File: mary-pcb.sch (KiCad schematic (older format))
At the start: 69 parts, among them SW1 SW_Push, SW2 Rotary_Encoder_Switch, U1 ATmega32U4-AU, Y1 16MHz

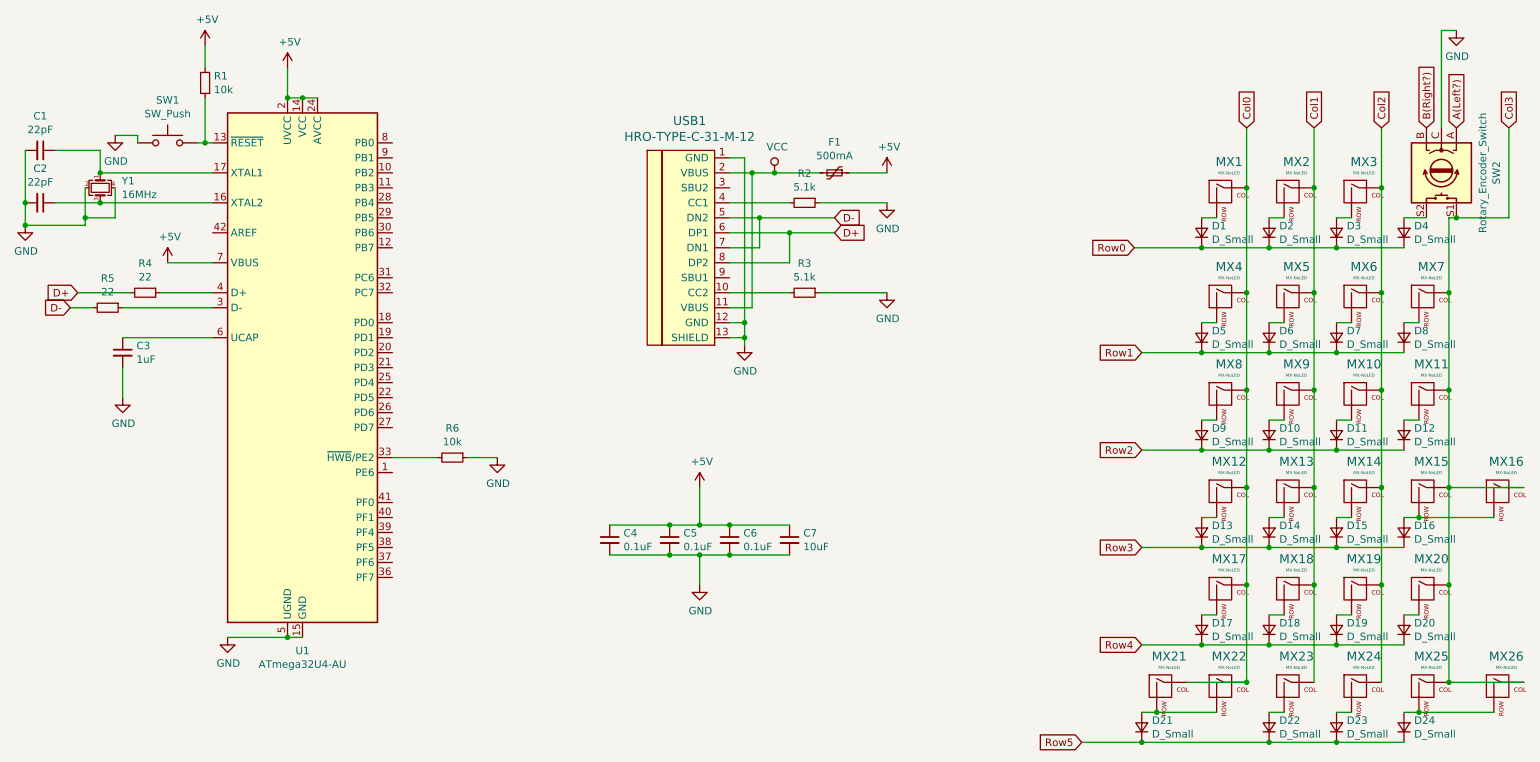
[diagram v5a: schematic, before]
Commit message: complete routing
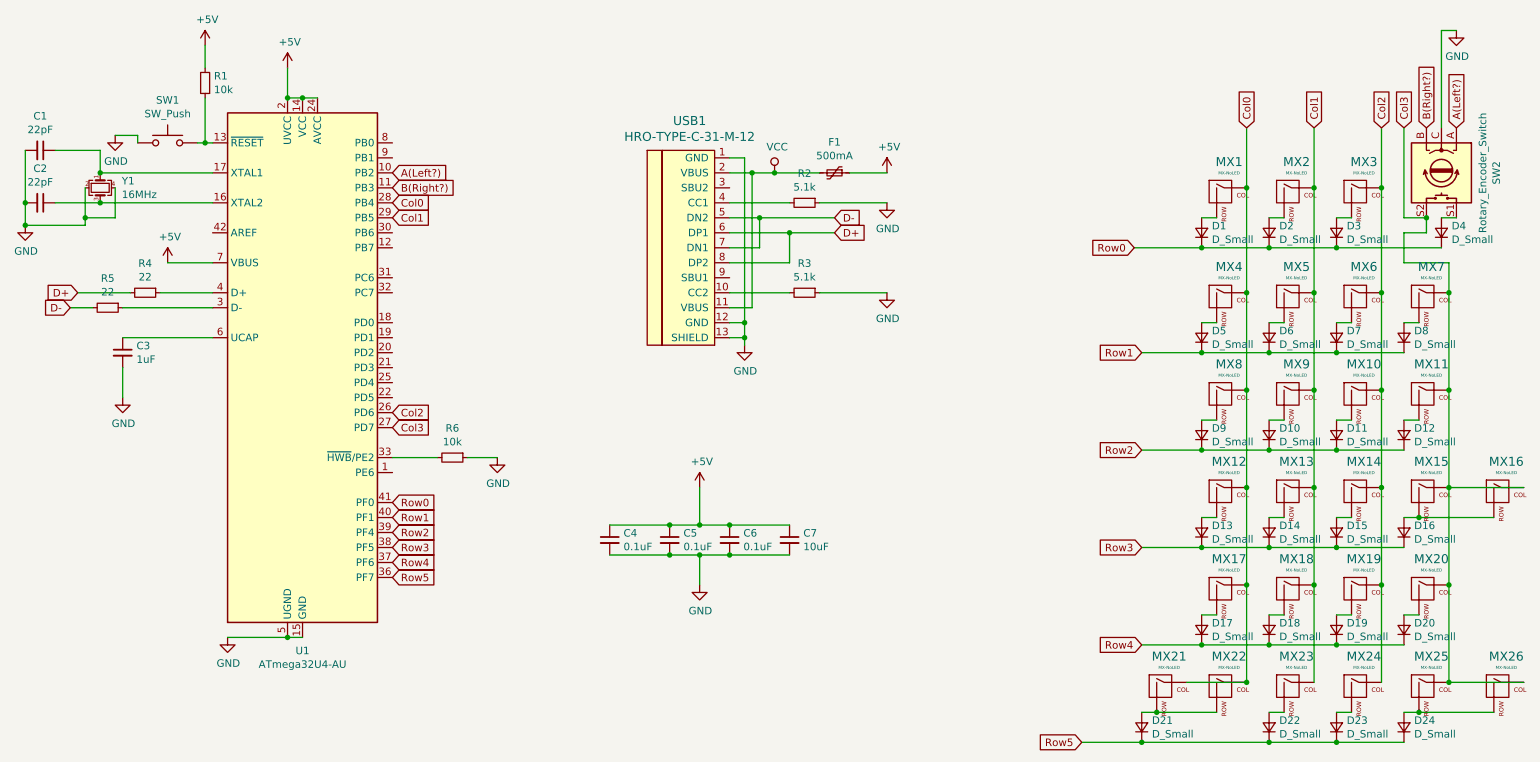
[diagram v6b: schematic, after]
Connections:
- net A(Left?): now also U1.10 (PB2)
- net B(Right?): now also U1.11 (PB3)
- net Col0: now also U1.28 (PB4)
- net Col1: now also U1.29 (PB5)
- net Col2: now also U1.26 (PD6)
- net Col3: now also SW2.S2, U1.27 (PD7); no longer SW2.S1
- net Row0: now also U1.41 (PF0)
- net Row1: now also U1.40 (PF1)
- net Row2: now also U1.39 (PF4)
- net Row3: now also U1.38 (PF5)
- net Row4: now also U1.37 (PF6)
- net Row5: now also U1.36 (PF7)
- net at D4.2 (A): now also SW2.S1; no longer SW2.S2
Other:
- moved on the sheet: D4
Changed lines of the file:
@@
 	0    1    1    0
 $EndComp
-$Comp
-L Device:D_Small D4
-U 1 1 5E3ADAEC
-P 10200 2050
-F 0 "D4" V 10246 1982 50  0000 R CNN
-F 1 "D_Small" V 10155 1982 50  0000 R CNN
-F 2 "Diode_SMD:D_SOD-123" V 10200 2050 50  0001 C CNN
-F 3 "~" V 10200 2050 50  0001 C CNN
-	1    10200 2050
-	0    -1   -1   0
-$EndComp
-Wire Wire Line
-	10350 1950 10200 1950
-Wire Wire Line
-	9750 2150 10200 2150
 Connection ~ 9750 2150
-Wire Wire Line
-	10550 1950 10900 1950
-Wire Wire Line
-	10900 1950 10900 1350
-Wire Wire Line
-	10550 1950 10500 1950
-Wire Wire Line
-	10500 1950 10500 2450
-Connection ~ 10550 1950
-Connection ~ 10500 2450
 Wire Wire Line
 	10500 2450 10500 3100
@@
 Text GLabel 10050 1350 1    50   Input ~ 0
 Col2
-Text GLabel 10900 1350 1    50   Input ~ 0
+Text GLabel 10200 1350 1    50   Input ~ 0
 Col3
 Text GLabel 10350 1350 1    50   Input ~ 0
@@
 Wire Wire Line
 	10450 700  10450 1350
+Wire Wire Line
+	9750 2150 10450 2150
+Wire Wire Line
+	10200 2250 10500 2250
+Wire Wire Line
+	10500 2250 10500 2450
+Connection ~ 10500 2450
+Text GLabel 3450 3850 2    50   Input ~ 0
+Row0
+Text GLabel 3450 3950 2    50   Input ~ 0
+Row1
+Text GLabel 3450 4050 2    50   Input ~ 0
+Row2
+Text GLabel 3450 4150 2    50   Input ~ 0
+Row3
+Text GLabel 3450 4250 2    50   Input ~ 0
+Row4
+Text GLabel 3450 4350 2    50   Input ~ 0
+Row5
+Text GLabel 3450 1850 2    50   Input ~ 0
+Col0
+Text GLabel 3450 1950 2    50   Input ~ 0
+Col1
+Text GLabel 3450 3250 2    50   Input ~ 0
+Col2
+Text GLabel 3450 3350 2    50   Input ~ 0
+Col3
+$Comp
+L Device:D_Small D4
+U 1 1 5E3ADAEC
+P 10450 2050
+F 0 "D4" V 10496 1982 50  0000 R CNN
+F 1 "D_Small" V 10405 1982 50  0000 R CNN
+F 2 "Diode_SMD:D_SOD-123" V 10450 2050 50  0001 C CNN
+F 3 "~" V 10450 2050 50  0001 C CNN
+	1    10450 2050
+	0    -1   -1   0
+$EndComp
+Wire Wire Line
+	10450 1950 10550 1950
+Wire Wire Line
+	10200 1350 10200 1950
+Wire Wire Line
+	10200 1950 10350 1950
+Wire Wire Line
+	10200 2250 10200 2050
+Wire Wire Line
+	10200 2050 10350 2050
+Wire Wire Line
+	10350 2050 10350 1950
+Connection ~ 10350 1950
+Text GLabel 3450 1650 2    50   Input ~ 0
+A(Left?)
+Text GLabel 3450 1750 2    50   Input ~ 0
+B(Right?)
 $EndSCHEMATC

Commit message: complete routing, upload renders
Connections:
- net A(Left?): now also U1.21 (PD3); no longer U1.10 (PB2)
- net B(Right?): now also U1.22 (PD5); no longer U1.11 (PB3)
- net Row0: now also U1.36 (PF7); no longer U1.41 (PF0)
- net Row1: now also U1.37 (PF6); no longer U1.40 (PF1)
- net Row2: now also U1.38 (PF5); no longer U1.39 (PF4)
- net Row3: now also U1.39 (PF4); no longer U1.38 (PF5)
- net Row4: now also U1.40 (PF1); no longer U1.37 (PF6)
- net Row5: now also U1.41 (PF0); no longer U1.36 (PF7)
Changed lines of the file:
@@
 	10500 2250 10500 2450
 Connection ~ 10500 2450
-Text GLabel 3450 3850 2    50   Input ~ 0
-Row0
-Text GLabel 3450 3950 2    50   Input ~ 0
-Row1
-Text GLabel 3450 4050 2    50   Input ~ 0
-Row2
-Text GLabel 3450 4150 2    50   Input ~ 0
-Row3
-Text GLabel 3450 4250 2    50   Input ~ 0
-Row4
-Text GLabel 3450 4350 2    50   Input ~ 0
-Row5
-Text GLabel 3450 1850 2    50   Input ~ 0
-Col0
-Text GLabel 3450 1950 2    50   Input ~ 0
-Col1
-Text GLabel 3450 3250 2    50   Input ~ 0
-Col2
-Text GLabel 3450 3350 2    50   Input ~ 0
-Col3
 $Comp
 L Device:D_Small D4
@@
 	10350 2050 10350 1950
 Connection ~ 10350 1950
-Text GLabel 3450 1650 2    50   Input ~ 0
+Text GLabel 3450 3850 2    50   Input ~ 0
+Row5
+Text GLabel 3450 3950 2    50   Input ~ 0
+Row4
+Text GLabel 3450 4050 2    50   Input ~ 0
+Row3
+Text GLabel 3450 4150 2    50   Input ~ 0
+Row2
+Text GLabel 3450 4250 2    50   Input ~ 0
+Row1
+Text GLabel 3450 4350 2    50   Input ~ 0
+Row0
+Text GLabel 3450 1850 2    50   Input ~ 0
+Col0
+Text GLabel 3450 3350 2    50   Input ~ 0
+Col3
+Text GLabel 3450 3250 2    50   Input ~ 0
+Col2
+Text GLabel 3450 1950 2    50   Input ~ 0
+Col1
+Text GLabel 3450 2950 2    50   Input ~ 0
 A(Left?)
-Text GLabel 3450 1750 2    50   Input ~ 0
+Text GLabel 3450 3150 2    50   Input ~ 0
 B(Right?)
 $EndSCHEMATC

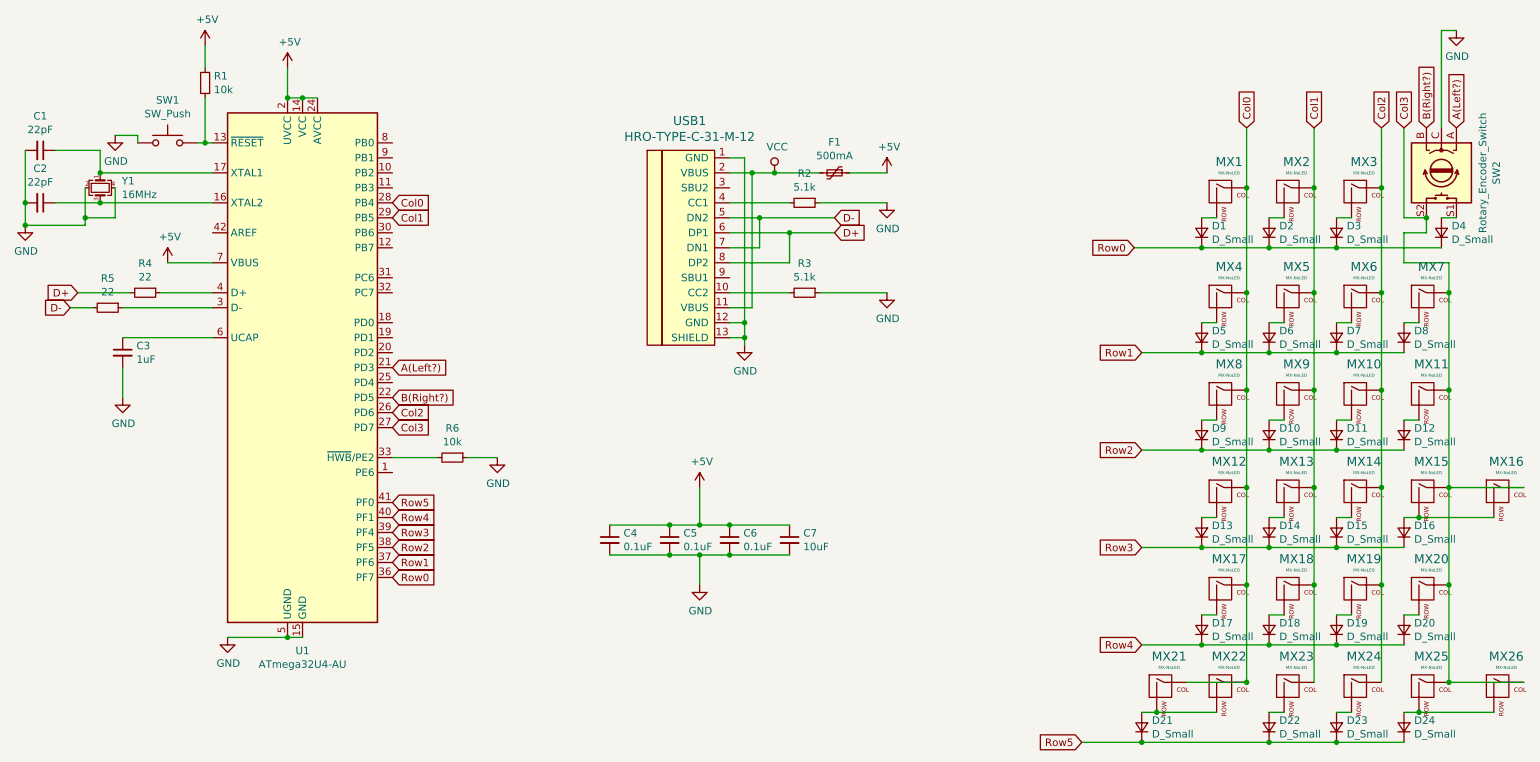
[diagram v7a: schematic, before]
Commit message: add esd protection, ground pours, via stitching
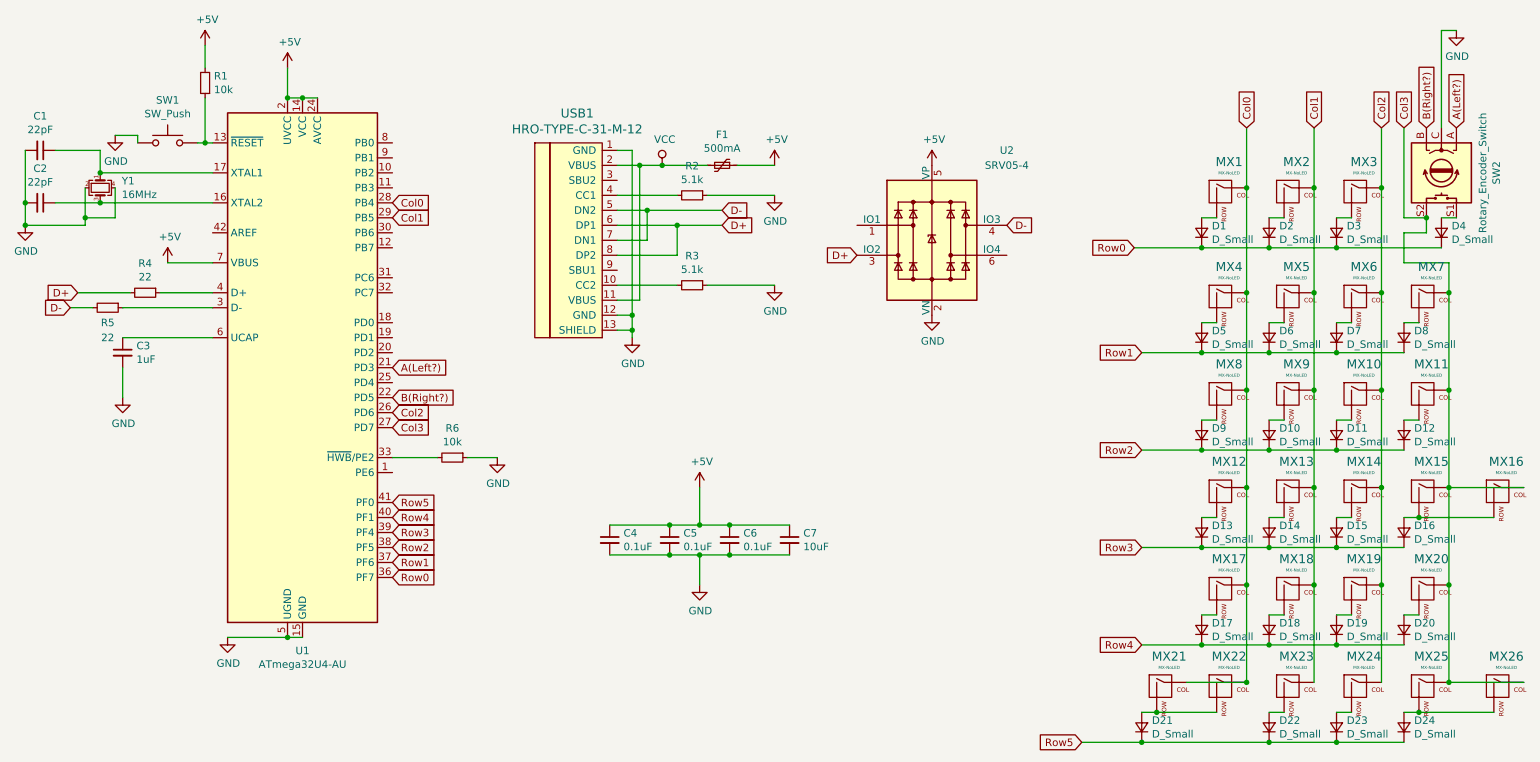
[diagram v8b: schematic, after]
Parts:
- added U2: SRV05-4, Package_TO_SOT_SMD:SOT-23-6, symbol Power_Protection:SRV05-4
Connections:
- net +5V: now also U2.5 (VP)
- net D+: now also U2.3 (IO2)
- net D-: now also U2.4 (IO3)
- net GND: now also U2.2 (VN)
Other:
- moved on the sheet: F1, R2, R3, USB1
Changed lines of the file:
@@
 U 1 1 5E0D915D
 P 1550 2550
-F 0 "R5" V 1354 2550 50  0000 C CNN
-F 1 "22" V 1445 2550 50  0000 C CNN
+F 0 "R5" V 1650 2550 50  0000 C CNN
+F 1 "22" V 1750 2550 50  0000 C CNN
 F 2 "Resistor_SMD:R_0805_2012Metric" H 1550 2550 50  0001 C CNN
 F 3 "~" H 1550 2550 50  0001 C CNN
@@
 L Type-C:HRO-TYPE-C-31-M-12 USB1
 U 1 1 5E154775
-P 5600 2100
-F 0 "USB1" H 5433 2897 60  0000 C CNN
-F 1 "HRO-TYPE-C-31-M-12" H 5433 2791 60  0000 C CNN
-F 2 "Type-C:HRO-TYPE-C-31-M-12" H 5600 2100 60  0001 C CNN
-F 3 "" H 5600 2100 60  0001 C CNN
-	1    5600 2100
+P 4850 2050
+F 0 "USB1" H 4683 2847 60  0000 C CNN
+F 1 "HRO-TYPE-C-31-M-12" H 4683 2741 60  0000 C CNN
+F 2 "Type-C:HRO-TYPE-C-31-M-12" H 4850 2050 60  0001 C CNN
+F 3 "" H 4850 2050 60  0001 C CNN
+	1    4850 2050
 	1    0    0    -1
 $EndComp
@@
 L Device:Polyfuse_Small F1
 U 1 1 5E1567C4
-P 6400 1650
-F 0 "F1" V 6195 1650 50  0000 C CNN
-F 1 "500mA" V 6286 1650 50  0000 C CNN
-F 2 "Fuse:Fuse_1206_3216Metric" H 6450 1450 50  0001 L CNN
-F 3 "~" H 6400 1650 50  0001 C CNN
-	1    6400 1650
+P 5650 1600
+F 0 "F1" V 5445 1600 50  0000 C CNN
+F 1 "500mA" V 5536 1600 50  0000 C CNN
+F 2 "Fuse:Fuse_1206_3216Metric" H 5700 1400 50  0001 L CNN
+F 3 "~" H 5650 1600 50  0001 C CNN
+	1    5650 1600
 	0    1    1    0
 $EndComp
@@
 L power:+5V #PWR0109
 U 1 1 5E15A63C
-P 6750 1650
-F 0 "#PWR0109" H 6750 1500 50  0001 C CNN
-F 1 "+5V" H 6765 1823 50  0000 C CNN
-F 2 "" H 6750 1650 50  0001 C CNN
-F 3 "" H 6750 1650 50  0001 C CNN
-	1    6750 1650
-	1    0    0    -1
-$EndComp
-Wire Wire Line
-	5700 1650 5850 1650
-Wire Wire Line
-	6500 1650 6750 1650
+P 6000 1600
+F 0 "#PWR0109" H 6000 1450 50  0001 C CNN
+F 1 "+5V" H 6015 1773 50  0000 C CNN
+F 2 "" H 6000 1600 50  0001 C CNN
+F 3 "" H 6000 1600 50  0001 C CNN
+	1    6000 1600
+	1    0    0    -1
+$EndComp
+Wire Wire Line
+	4950 1600 5100 1600
+Wire Wire Line
+	5750 1600 6000 1600
 $Comp
 L power:VCC #PWR0110
 U 1 1 5E15C909
-P 6000 1650
-F 0 "#PWR0110" H 6000 1500 50  0001 C CNN
-F 1 "VCC" H 6017 1823 50  0000 C CNN
-F 2 "" H 6000 1650 50  0001 C CNN
-F 3 "" H 6000 1650 50  0001 C CNN
-	1    6000 1650
-	1    0    0    -1
-$EndComp
-Connection ~ 6000 1650
-Wire Wire Line
-	6000 1650 6300 1650
-Text GLabel 6400 2050 2    50   Input ~ 0
+P 5250 1600
+F 0 "#PWR0110" H 5250 1450 50  0001 C CNN
+F 1 "VCC" H 5267 1773 50  0000 C CNN
+F 2 "" H 5250 1600 50  0001 C CNN
+F 3 "" H 5250 1600 50  0001 C CNN
+	1    5250 1600
+	1    0    0    -1
+$EndComp
+Connection ~ 5250 1600
+Wire Wire Line
+	5250 1600 5550 1600
+Text GLabel 5650 2000 2    50   Input ~ 0
 D+
 Wire Wire Line
-	5700 2050 6100 2050
-Wire Wire Line
-	5700 2250 6100 2250
-Wire Wire Line
-	6100 2250 6100 2050
-Connection ~ 6100 2050
-Wire Wire Line
-	6100 2050 6400 2050
-Text GLabel 6400 1950 2    50   Input ~ 0
+	4950 2000 5350 2000
+Wire Wire Line
+	4950 2200 5350 2200
+Wire Wire Line
+	5350 2200 5350 2000
+Connection ~ 5350 2000
+Wire Wire Line
+	5350 2000 5650 2000
+Text GLabel 5650 1900 2    50   Input ~ 0
 D-
 Wire Wire Line
-	5700 1950 5900 1950
-Wire Wire Line
-	5700 2150 5900 2150
-Wire Wire Line
-	5900 2150 5900 1950
-Connection ~ 5900 1950
-Wire Wire Line
-	5900 1950 6400 1950
+	4950 1900 5150 1900
+Wire Wire Line
+	4950 2100 5150 2100
+Wire Wire Line
+	5150 2100 5150 1900
+Connection ~ 5150 1900
+Wire Wire Line
+	5150 1900 5650 1900
 $Comp
 L power:GND #PWR0111
 U 1 1 5E164B62
-P 5800 2800
-F 0 "#PWR0111" H 5800 2550 50  0001 C CNN
-F 1 "GND" H 5805 2627 50  0000 C CNN
-F 2 "" H 5800 2800 50  0001 C CNN
-F 3 "" H 5800 2800 50  0001 C CNN
-	1    5800 2800
-	1    0    0    -1
-$EndComp
-Wire Wire Line
-	5700 1550 5800 1550
-Wire Wire Line
-	5800 1550 5800 2650
-Wire Wire Line
-	5700 2650 5800 2650
-Connection ~ 5800 2650
-Wire Wire Line
-	5800 2650 5800 2750
-Wire Wire Line
-	5700 2750 5800 2750
-Connection ~ 5800 2750
-Wire Wire Line
-	5800 2750 5800 2800
-Wire Wire Line
-	5700 2550 5850 2550
-Wire Wire Line
-	5850 2550 5850 1650
-Connection ~ 5850 1650
-Wire Wire Line
-	5850 1650 6000 1650
+P 5050 2750
+F 0 "#PWR0111" H 5050 2500 50  0001 C CNN
+F 1 "GND" H 5055 2577 50  0000 C CNN
+F 2 "" H 5050 2750 50  0001 C CNN
+F 3 "" H 5050 2750 50  0001 C CNN
+	1    5050 2750
+	1    0    0    -1
+$EndComp
+Wire Wire Line
+	4950 1500 5050 1500
+Wire Wire Line
+	5050 1500 5050 2600
+Wire Wire Line
+	4950 2600 5050 2600
+Connection ~ 5050 2600
+Wire Wire Line
+	5050 2600 5050 2700
+Wire Wire Line
+	4950 2700 5050 2700
+Connection ~ 5050 2700
+Wire Wire Line
+	5050 2700 5050 2750
+Wire Wire Line
+	4950 2500 5100 2500
+Wire Wire Line
+	5100 2500 5100 1600
+Connection ~ 5100 1600
+Wire Wire Line
+	5100 1600 5250 1600
 $Comp
 L power:GND #PWR0112
 U 1 1 5E17016B
-P 6750 1850
-F 0 "#PWR0112" H 6750 1600 50  0001 C CNN
-F 1 "GND" H 6755 1677 50  0000 C CNN
-F 2 "" H 6750 1850 50  0001 C CNN
-F 3 "" H 6750 1850 50  0001 C CNN
-	1    6750 1850
+P 6000 1800
+F 0 "#PWR0112" H 6000 1550 50  0001 C CNN
+F 1 "GND" H 6005 1627 50  0000 C CNN
+F 2 "" H 6000 1800 50  0001 C CNN
+F 3 "" H 6000 1800 50  0001 C CNN
+	1    6000 1800
 	1    0    0    -1
 $EndComp
@@
 L Device:R_Small R2
 U 1 1 5E172396
-P 6200 1850
-F 0 "R2" V 6004 1850 50  0000 C CNN
-F 1 "5.1k" V 6095 1850 50  0000 C CNN
-F 2 "Resistor_SMD:R_0805_2012Metric" H 6200 1850 50  0001 C CNN
-F 3 "~" H 6200 1850 50  0001 C CNN
-	1    6200 1850
+P 5450 1800
+F 0 "R2" V 5254 1800 50  0000 C CNN
+F 1 "5.1k" V 5345 1800 50  0000 C CNN
+F 2 "Resistor_SMD:R_0805_2012Metric" H 5450 1800 50  0001 C CNN
+F 3 "~" H 5450 1800 50  0001 C CNN
+	1    5450 1800
 	0    1    1    0
 $EndComp
 Wire Wire Line
-	5700 1850 6100 1850
-Wire Wire Line
-	6300 1850 6750 1850
+	4950 1800 5350 1800
+Wire Wire Line
+	5550 1800 6000 1800
 $Comp
 L Device:R_Small R3
 U 1 1 5E175B75
-P 6200 2450
-F 0 "R3" V 6004 2450 50  0000 C CNN
-F 1 "5.1k" V 6095 2450 50  0000 C CNN
-F 2 "Resistor_SMD:R_0805_2012Metric" H 6200 2450 50  0001 C CNN
-F 3 "~" H 6200 2450 50  0001 C CNN
-	1    6200 2450
+P 5450 2400
+F 0 "R3" V 5254 2400 50  0000 C CNN
+F 1 "5.1k" V 5345 2400 50  0000 C CNN
+F 2 "Resistor_SMD:R_0805_2012Metric" H 5450 2400 50  0001 C CNN
+F 3 "~" H 5450 2400 50  0001 C CNN
+	1    5450 2400
 	0    1    1    0
 $EndComp
@@
 L power:GND #PWR0113
 U 1 1 5E175EA6
-P 6750 2450
-F 0 "#PWR0113" H 6750 2200 50  0001 C CNN
-F 1 "GND" H 6755 2277 50  0000 C CNN
-F 2 "" H 6750 2450 50  0001 C CNN
-F 3 "" H 6750 2450 50  0001 C CNN
-	1    6750 2450
-	1    0    0    -1
-$EndComp
-Wire Wire Line
-	5700 2450 6100 2450
-Wire Wire Line
-	6300 2450 6750 2450
+P 6000 2400
+F 0 "#PWR0113" H 6000 2150 50  0001 C CNN
+F 1 "GND" H 6005 2227 50  0000 C CNN
+F 2 "" H 6000 2400 50  0001 C CNN
+F 3 "" H 6000 2400 50  0001 C CNN
+	1    6000 2400
+	1    0    0    -1
+$EndComp
+Wire Wire Line
+	4950 2400 5350 2400
+Wire Wire Line
+	5550 2400 6000 2400
 Wire Wire Line
 	5500 4000 5300 4000
@@
 Text GLabel 3450 3150 2    50   Input ~ 0
 B(Right?)
+$Comp
+L Power_Protection:SRV05-4 U2
+U 1 1 5E6936CC
+P 7050 2100
+F 0 "U2" H 7550 2700 50  0000 C CNN
+F 1 "SRV05-4" H 7550 2600 50  0000 C CNN
+F 2 "Package_TO_SOT_SMD:SOT-23-6" H 7750 1650 50  0001 C CNN
+F 3 "http://www.onsemi.com/pub/Collateral/SRV05-4-D.PDF" H 7050 2100 50  0001 C CNN
+	1    7050 2100
+	1    0    0    -1
+$EndComp
+$Comp
+L power:+5V #PWR0117
+U 1 1 5E696583
+P 7050 1600
+F 0 "#PWR0117" H 7050 1450 50  0001 C CNN
+F 1 "+5V" H 7065 1773 50  0000 C CNN
+F 2 "" H 7050 1600 50  0001 C CNN
+F 3 "" H 7050 1600 50  0001 C CNN
+	1    7050 1600
+	1    0    0    -1
+$EndComp
+$Comp
+L power:GND #PWR0118
+U 1 1 5E697FA4
+P 7050 2600
+F 0 "#PWR0118" H 7050 2350 50  0001 C CNN
+F 1 "GND" H 7055 2427 50  0000 C CNN
+F 2 "" H 7050 2600 50  0001 C CNN
+F 3 "" H 7050 2600 50  0001 C CNN
+	1    7050 2600
+	1    0    0    -1
+$EndComp
+Text GLabel 6550 2200 0    50   Input ~ 0
+D+
+Text GLabel 7550 2000 2    50   Input ~ 0
+D-
 $EndSCHEMATC
